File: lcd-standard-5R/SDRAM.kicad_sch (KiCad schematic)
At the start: 8 parts, among them U4 MT48LC16M16A2P

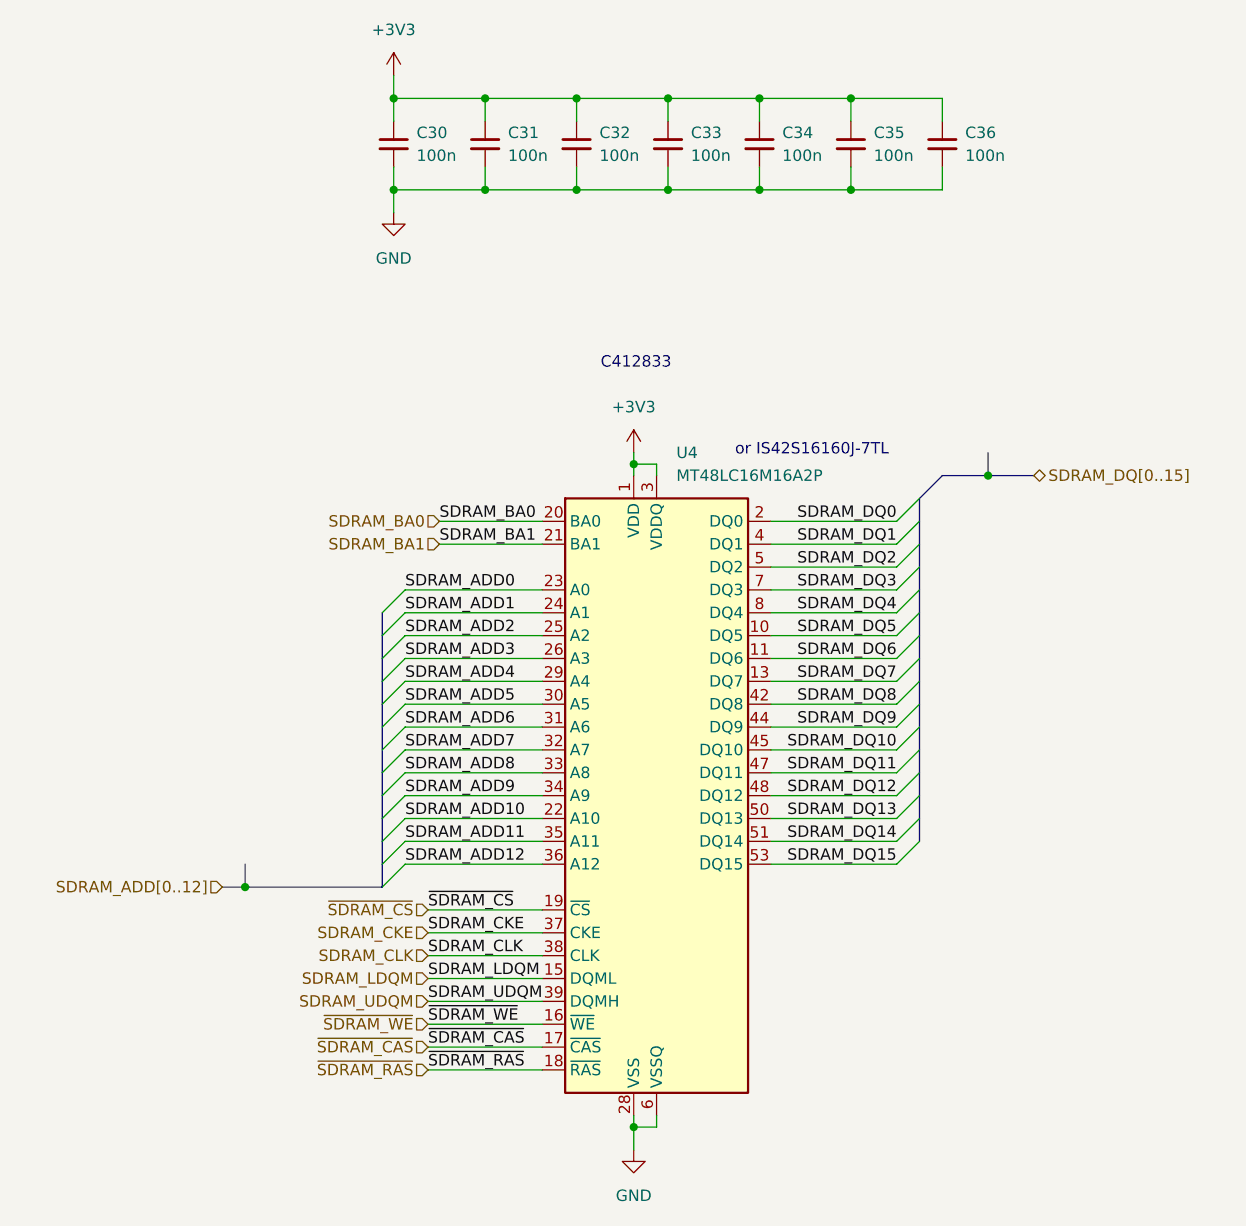
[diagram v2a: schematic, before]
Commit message: relocate SDRAM & QSPI Flash
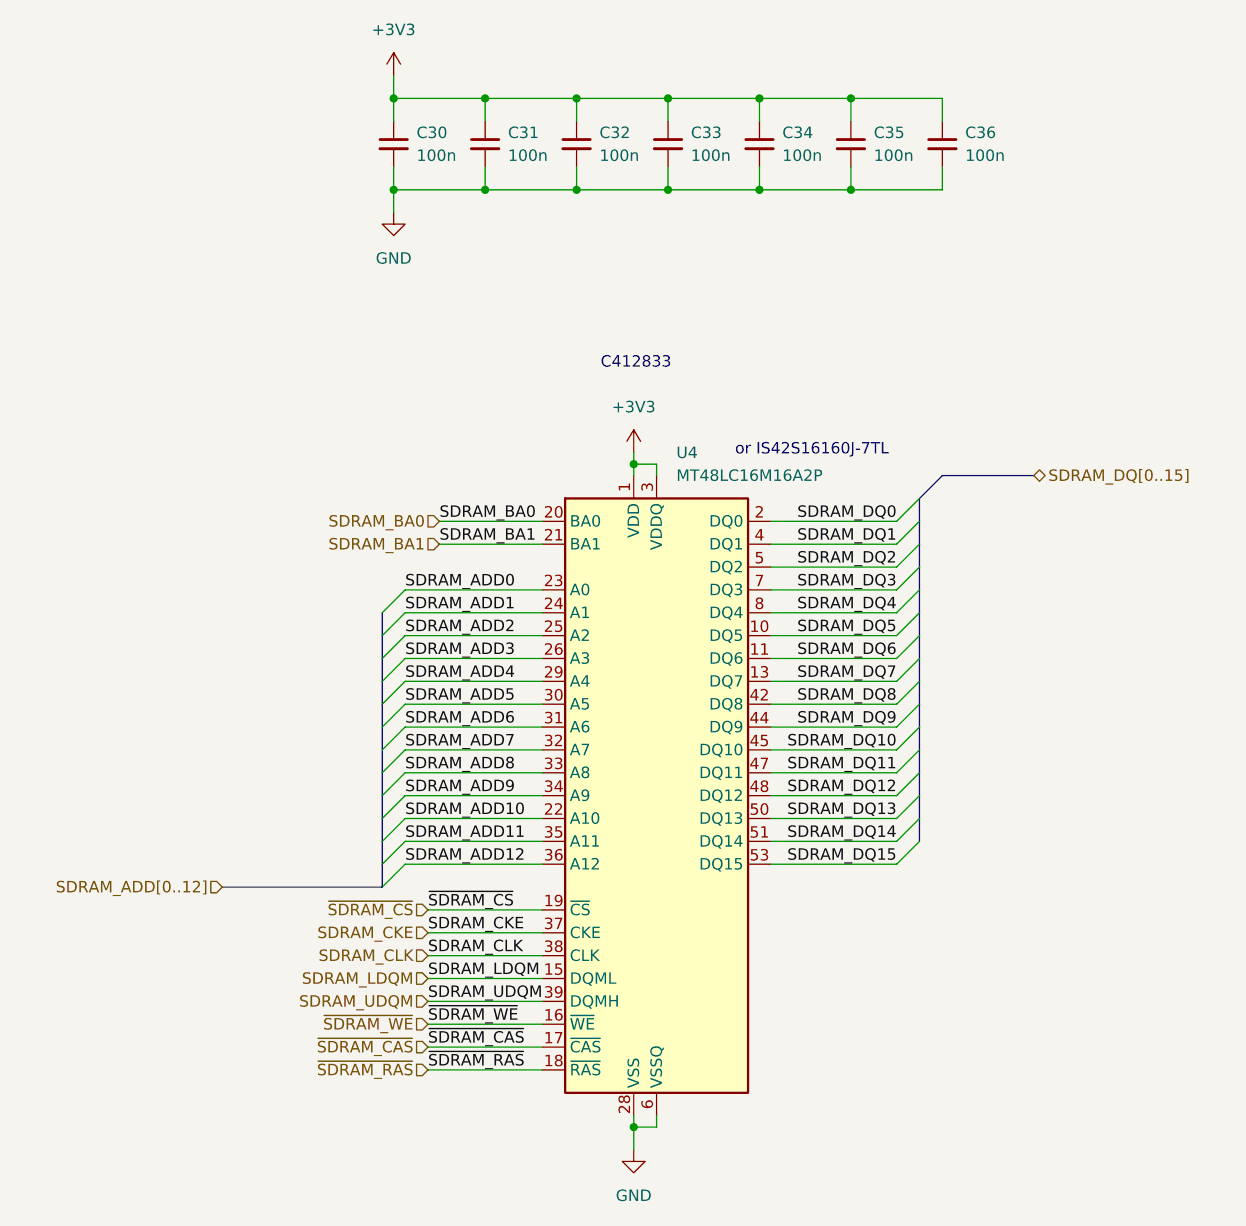
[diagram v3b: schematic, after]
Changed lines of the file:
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@@
-	)
-	(junction
-		(at 181.61 80.01)
-		(diameter 0)
-		(color 0 0 0 0)
-	)
-	(junction
-		(at 99.06 125.73)
-		(diameter 0)
-		(color 0 0 0 0)
 	)
 	(junction
@@
 	(bus
 		(pts
-			(xy 176.53 80.01) (xy 181.61 80.01)
+			(xy 176.53 80.01) (xy 186.69 80.01)
 		)
 		(stroke
@@
 	(bus
 		(pts
-			(xy 181.61 80.01) (xy 186.69 80.01)
-		)
-		(stroke
-			(width 0)
-			(type default)
-		)
-	)
-	(bus
-		(pts
 			(xy 173.99 110.49) (xy 173.99 107.95)
 		)
@@
 		)
 	)
-	(bus
-		(pts
-			(xy 181.61 77.47) (xy 181.61 80.01)
-		)
-		(stroke
-			(width 0)
-			(type default)
-		)
-	)
 	(wire
 		(pts
@@
 		)
 	)
-	(bus
-		(pts
-			(xy 99.06 123.19) (xy 99.06 125.73)
-		)
-		(stroke
-			(width 0)
-			(type default)
-		)
-	)
 	(wire
 		(pts
@@
 	(bus
 		(pts
-			(xy 99.06 125.73) (xy 114.3 125.73)
+			(xy 96.52 125.73) (xy 114.3 125.73)
 		)
 		(stroke
@@
 		(pts
 			(xy 114.3 123.19) (xy 114.3 125.73)
-		)
-		(stroke
-			(width 0)
-			(type default)
-		)
-	)
-	(bus
-		(pts
-			(xy 96.52 125.73) (xy 99.06 125.73)
 		)
 		(stroke
@@
 		)
 	)
+	(rule_area
+		(polyline
+			(pts
+				(xy 96.52 82.55) (xy 186.69 82.55) (xy 186.69 148.59) (xy 96.52 148.59)
+			)
+			(stroke
+				(width 0)
+				(type dash)
+			)
+			(fill
+				(type none)
+			)
+		)
+	)
 	(netclass_flag ""
 		(length 2.54)
 		(shape round)
-		(at 99.06 123.19 0)
+		(at 102.87 82.55 0)
 		(fields_autoplaced yes)
 		(effects
@@
 			(justify left bottom)
 		)
-		(property "Netclass" "SDRAM_ADDRESS"
-			(at 98.3615 120.65 0)
+		(property "Netclass" "SDRAM"
+			(at 103.5685 80.01 0)
+			(effects
+				(font
+					(size 1.27 1.27)
+				)
+				(justify left)
+			)
+		)
+		(property "Component Class" ""
+			(at -110.49 -22.86 0)
 			(effects
 				(font
@@
 					(italic yes)
 				)
-				(justify right)
-			)
-		)
-	)
-	(netclass_flag ""
-		(length 2.54)
-		(shape round)
-		(at 181.61 77.47 0)
-		(fields_autoplaced yes)
-		(effects
-			(font
-				(size 1.27 1.27)
-			)
-			(justify left bottom)
-		)
-		(property "Netclass" "SDRAM_DATA"
-			(at 182.3085 74.93 0)
-			(effects
-				(font
-					(size 1.27 1.27)
-					(italic yes)
-				)
-				(justify left)
-			)
-		)
+			)
+		)
